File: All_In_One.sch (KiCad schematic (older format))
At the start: 20 parts

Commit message: complete schematic
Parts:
- removed D?: D_Zener, symbol Device:D_Zener
- removed D?: DIODE, symbol pspice:DIODE
- removed U? (x2): L298, symbol Prashant_library:L298
- added D? (x2): DIODE, symbol pspice:DIODE
- added D?: D_Zener, symbol Device:D_Zener
- added J?: Stepper_xaxis, symbol Connector:Conn_01x04_Female
- added J?: Stepper_yaxis, symbol Connector:Conn_01x04_Female
- added U? (x2): L298, symbol l298:L298
- A?: value Pololu_Breakout_A4988 -> Y_AXIS
- A?: value Pololu_Breakout_A4988 -> X_AXIS
- J?: value Conn_01x04_Female -> Bluetooth
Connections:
- net labels added: +12V, +24V, +5V, M0_1, M0_2, M0_EN, M0_IN1, M0_IN2, M1_1, M1_2, M1_EN, M1_IN1, M1_IN2, M2_1, M2_2, M2_EN, M2_IN1, M2_IN2, M3_1, M3_2, M3_EN, M3_IN1, M3_IN2, P_BACK, P_DOWN, P_FRONT, P_LEFT, P_RIGHT, P_UP, RX, TX, X_1A, X_1B, X_2A, X_2B, Y_1A, Y_1B, Y_2A, Y_2B, dirx, diry, en_x, en_y, stepx, stepy
- net labels removed: 12V, 24V, 5V
- wire segments 34 -> 125
- no-connect marks 0 -> 1
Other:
- note added: "5V REGULATOR"
- note added: "ARDUINO CONTROLLER\n"
- note added: "ARM PROXY\n"
- note added: "BASE MOTOR DRIVER"
- note added: "BASE PROXY\n"
- note added: "BLUETOOTH"
- note added: "STEPPER DRIVER ( A4988 )\n"
- note added: "STEPPER MOTOR\n"
- moved on the sheet: 1.2k

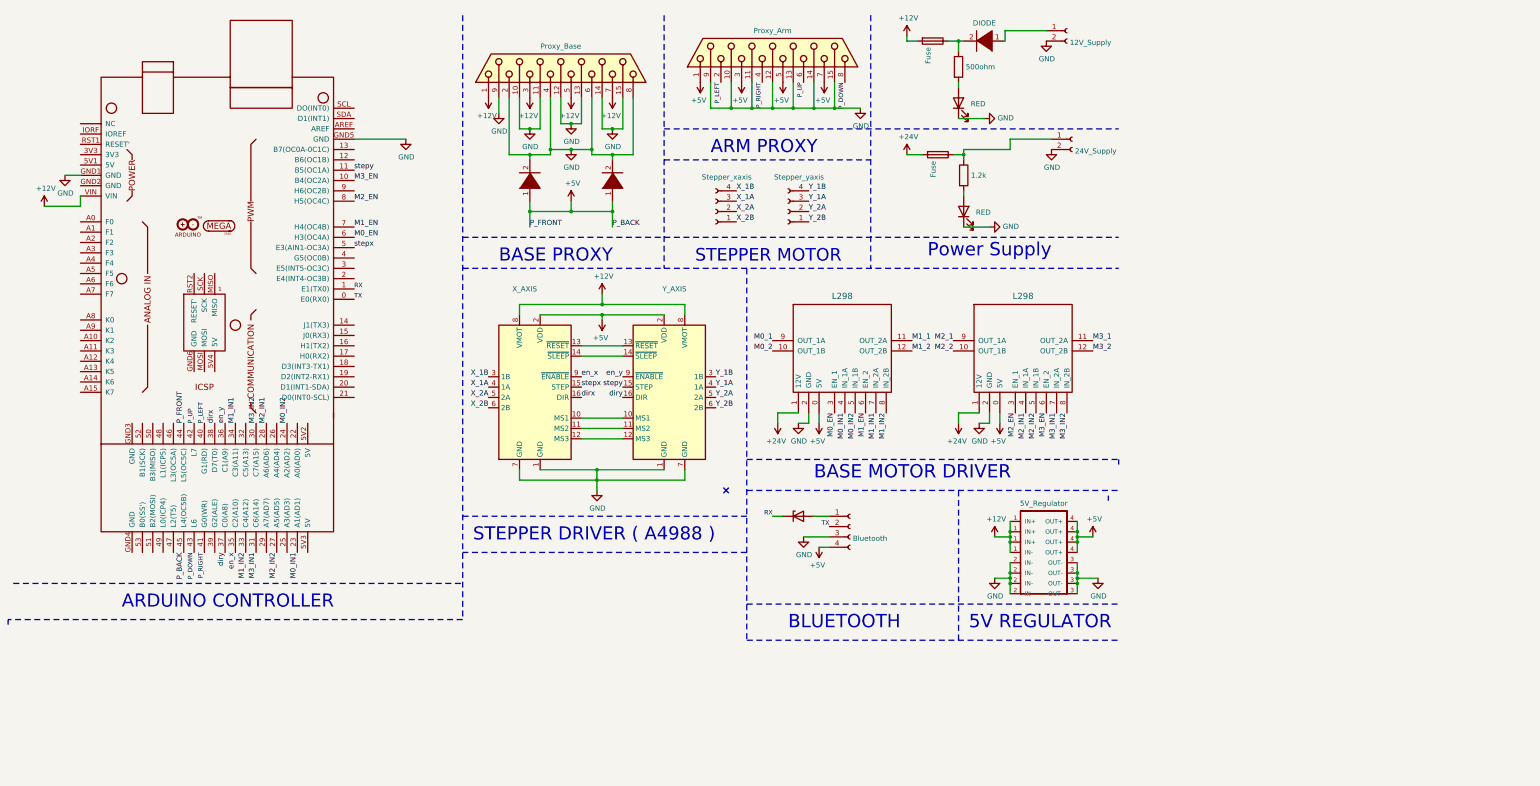
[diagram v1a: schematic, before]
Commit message: seperate ground for base motor and rest using opto-coupler
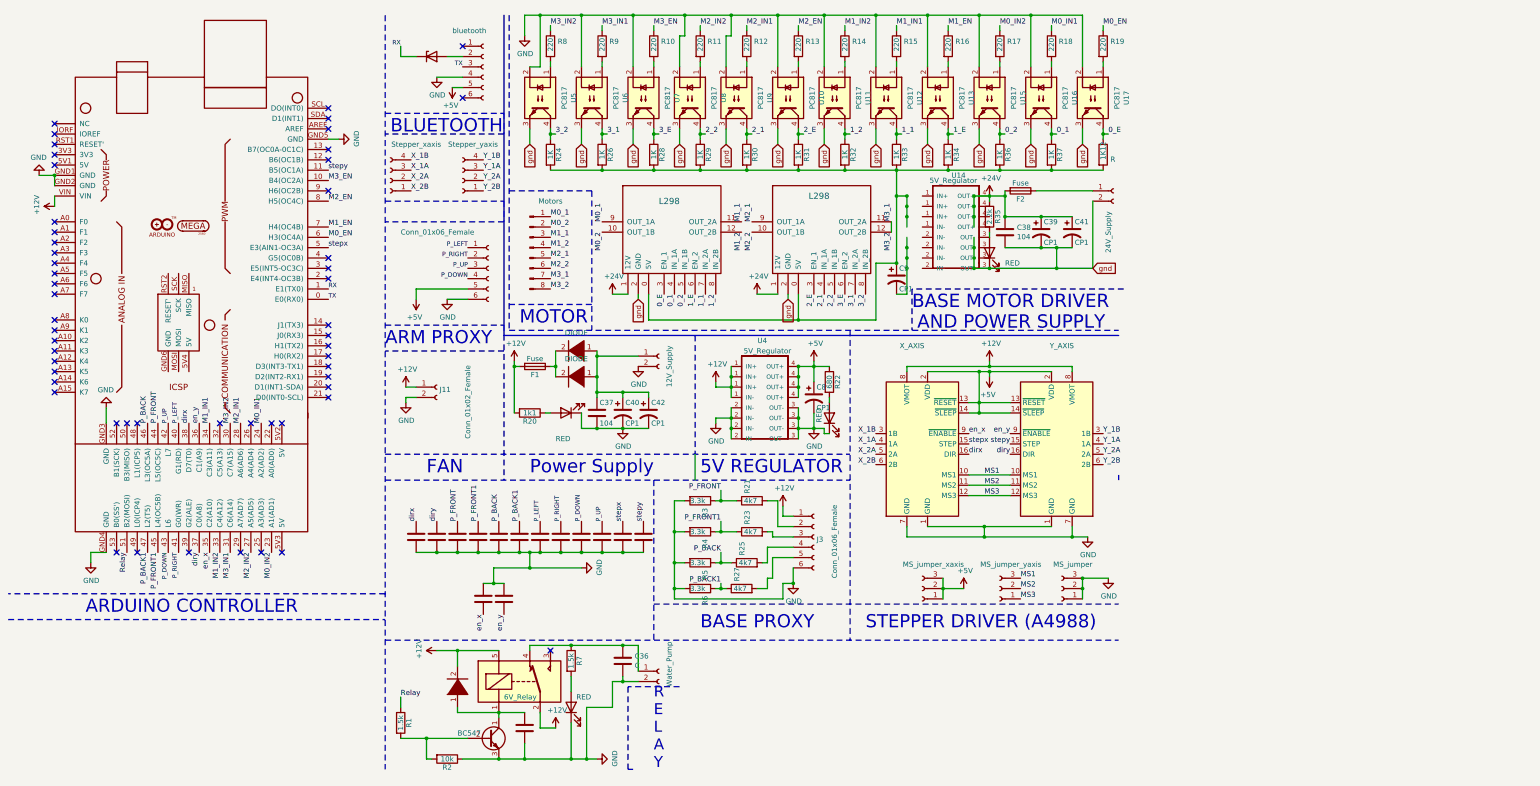
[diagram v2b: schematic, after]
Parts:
- removed D? (x2): DIODE, symbol pspice:DIODE
- removed J?: Bluetooth, symbol Connector:Conn_01x04_Female
- removed J?: Proxy_Base, symbol Connector:DB15_Female
- removed J?: Proxy_Arm, symbol Connector:DB15_Female
- added 1K12: R, modFiles:Resistor_small, symbol Device:R
- added C1, C13, C15, C2, C25, C27, C29, C3, C31, C33, C35, C36, C4, C5, C6, C7: C, modFiles:Capacitor_Disc_Small, symbol Device:C
- added C37, C38: 104, modFiles:Capacitor_Disc_Small, symbol Device:C
- added C39, C42: CP1, modFiles:Capacitor_10uF, symbol Device:CP1
- added C40, C41, C8, C9: CP1, modFiles:Capacitor_1000uF, symbol Device:CP1
- added D1, D3: DIODE, modFiles:Diode_Medium, symbol pspice:DIODE
- added D11, D2: RED, modFiles:LED_D3.0mm, symbol Device:LED
- added J1: MS_jumper_xaxis, symbol Connector:Conn_01x03_Female
- added J10: Motors, symbol Connector:Conn_01x08_Male
- added J11: Conn_01x02_Female, symbol Connector:Conn_01x02_Female
- added J2: MS_jumper_yaxis, symbol Connector:Conn_01x03_Female
- added J3, J8: Conn_01x06_Female, symbol Connector:Conn_01x06_Female
- added J4: Water_Pump, symbol Connector:Conn_01x02_Female
- added J5: MS_jumper, symbol Connector:Conn_01x03_Female
- added J9: bluetooth, symbol Connector:Conn_01x06_Female
- added Q1: BC547, Package_TO_SOT_THT:TO-92_Inline, symbol Transistor_BJT:BC547
- added R1, R7: 1.5k, modFiles:Resistor_small, symbol Device:R
- added R10, R11, R12, R13, R14, R15, R16, R17, R18, R19, R8, R9: 220, modFiles:Resistor_small, symbol Device:R
- added R2: 10k, modFiles:Resistor_small, symbol Device:R
- added R21, R23, R25, R27: 4k7, modFiles:Resistor_small, symbol Device:R
- added R22: 680, modFiles:Resistor_small, symbol Device:R
- added R24, R26, R28, R29, R30, R31, R32, R33, R34, R36, R37: 1K, modFiles:Resistor_small, symbol Device:R
- added R3, R4, R5, R6: 3.3k, modFiles:Resistor_small, symbol Device:R
- added Rly1: 6V_Relay, symbol Prashant_library:6V_Relay
- added U10, U11, U12, U13, U15, U16, U17, U5, U6, U7, U8, U9: PC817, Package_DIP:DIP-4_W7.62mm, symbol Isolator:PC817
- added U14: 5V_Regulator, modFiles:Buck 5A, symbol BUCK_Controller:BUCK
- A1, A2: renamed from A?; footprint Module:Pololu_Breakout-16_15.2x20.3mm -> modFiles:A4998
- D10: renamed from D?; footprint (none) -> modFiles:Diode_Medium
- D7: renamed from D?; footprint (none) -> Diode_THT:D_T-1_P5.08mm_Horizontal
- D8, D9: renamed from D?; footprint (none) -> modFiles:LED_D3.0mm
- F1, F2: renamed from F?; footprint (none) -> modFiles:Fuse_Holder
- R20: renamed from 500ohm; value R -> 1k1; footprint (none) -> modFiles:Resistor_small
- R35: renamed from 1.2k; value R -> 2.2k; footprint (none) -> modFiles:Resistor_small
- U2, U3: renamed from U?; footprint (none) -> modFiles:L298
- U4: renamed from U?; footprint (none) -> modFiles:Buck_Regulator
- d1: renamed from d; footprint (none) -> modFiles:Solar_Connector
- d2: renamed from d?; footprint (none) -> modFiles:Solar_Connector
- gave numbers to parts that had none: 3
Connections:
- net M3_2 is gone; now on net M3_1: U3.12 (OUT_2B)
- net +12V: now also R20.2, D1.2 (A), J11.1 (Pin_1), J3.1 (Pin_1), Rly1.2, Rly1.5
- net +24V: now also R35.1, C38.1, C39.1, C41.1, U14.4 (OUT+)
- net +5V: now also A1.13 (~RESET), A1.14 (~SLEEP), A2.13 (~RESET), A2.14 (~SLEEP), C8.1, J1.1 (Pin_1), J1.2 (Pin_2), J1.3 (Pin_3), J8.5 (Pin_5), J9.5 (Pin_5), R22.1; no longer U1.44 (L5(OC5C)), U1.45 (L4(OC5B)), U2.0 (5V), U3.0 (5V)
- net GND: now also U1.GND2 (GND), U1.GND3 (GND), U1.GND4 (GND), C1.2, C13.2, C15.2, C2.2, C25.2, C27.2, C29.2, C3.2, C31.2, C33.2, C35.2, C36.2, C37.2, C4.2, C40.2, C42.2, C5.2, C6.2, C7.2, C8.2, D11.1 (K), D2.1 (K), J11.2 (Pin_2), J3.6 (Pin_6), J4.2 (Pin_2), J5.1 (Pin_1), J5.2 (Pin_2), J5.3 (Pin_3), J8.6 (Pin_6), J9.4 (Pin_4), Q1.3 (E), R2.1, R3.2, R4.2, R5.2, R6.2, U10.2, U11.2, U12.2, U13.2, U15.2, U16.2, U17.2, U5.2, U6.2, U7.2, U8.2, U9.2; no longer D8.1 (K), U2.2 (GND), U3.2 (GND), d2.2 (Pin_2)
- net M0_1: now also J10.1 (Pin_1)
- net M0_2: now also J10.2 (Pin_2)
- net M0_EN: now also R19.1; no longer U2.3 (EN_1)
- net M0_IN1: now also U1.24 (A2(AD2)), R18.1; no longer U1.23 (A1(AD1)), U2.4 (IN_1A)
- net M0_IN2: now also U1.23 (A1(AD1)), R17.1; no longer U1.24 (A2(AD2)), U2.5 (IN_1B)
- net M1_1: now also J10.3 (Pin_3)
- net M1_2: now also J10.4 (Pin_4)
- net M1_EN: now also R16.1; no longer U2.6 (EN_2)
- net M1_IN1: now also R15.1; no longer U2.7 (IN_2A)
- net M1_IN2: now also R14.1; no longer U2.8 (IN_2B)
- net M2_1: now also J10.5 (Pin_5)
- net M2_2: now also J10.6 (Pin_6)
- net M2_EN: now also R13.1; no longer U3.3 (EN_1)
- net M2_IN1: now also R12.1; no longer U3.4 (IN_1A)
- net M2_IN2: now also R11.1; no longer U3.5 (IN_1B)
- net M3_1: now also J10.7 (Pin_7), J10.8 (Pin_8)
- net M3_EN: now also R10.1; no longer U3.6 (EN_2)
- net M3_IN1: now also R9.1; no longer U3.7 (IN_2A)
- net M3_IN2: now also R8.1; no longer U3.8 (IN_2B)
- net P_DOWN: now also C29.1, J8.4 (Pin_4)
- net P_LEFT: now also C25.1, J8.1 (Pin_1)
- net P_RIGHT: now also C27.1, J8.2 (Pin_2)
- net P_UP: now also C31.1, J8.3 (Pin_3)
- net TX: now also J9.3 (Pin_3)
- net dirx: now also C13.1
- net diry: now also C15.1
- net en_x: now also C3.1
- net en_y: now also C1.1
- net stepx: now also C33.1
- net stepy: now also C35.1
- net at D7.2 (A): now also J9.2 (Pin_2)
- net at D10.2 (A), F1.1: now also D3.2 (A); no longer R20.1
- net at D10.1 (K), d1.1 (Pin_1): now also C37.1, C40.1, C42.1, D3.1 (K)
- net MS1: now reaches A1.10 (MS1), A2.10 (MS1)
- net MS1: now also J2.3 (Pin_3)
- net MS2: now reaches A1.11 (MS2), A2.11 (MS2)
- net MS2: now also J2.2 (Pin_2)
- net MS3: now reaches A1.12 (MS3), A2.12 (MS3)
- net MS3: now also J2.1 (Pin_1)
- net at D9.2 (A): now also R20.1; no longer R20.2
- net at F2.1, d2.1 (Pin_1): no longer R35.1
- net at D8.2 (A), R35.2: now also U14.3 (OUT-)
- net P_BACK: now reaches U1.46 (L3(OC5A))
- net P_BACK: now also C5.1, R25.1, R5.1
- net P_BACK1: now reaches U1.47 (L2(T5))
- net P_BACK1: now also C6.1, R27.1, R6.1
- net Relay: now reaches U1.51 (B2(MOSI))
- net Relay: now also R1.1
- new net: 1K12.2, C9.1, R24.2, R26.2, R28.2, R29.2, R30.2, R31.2, R32.2, R33.2, R34.2, R36.2, R37.2, U2.0 (5V), U3.0 (5V)
- new net: R19.2, U17.1
- new net: D11.2 (A), R22.2
- new net: R18.2, U16.1
- new net: R17.2, U15.1
- new net: R16.2, U13.1
- new net: R15.2, U12.1
- new net: R14.2, U11.1
- new net: R13.2, U10.1
- new net: R12.2, U9.1
- new net: R11.2, U8.1
- new net: R10.2, U7.1
- new net: R9.2, U6.1
- new net: R8.2, U5.1
- new net: C7.1, D1.1 (K), Q1.1 (C), Rly1.1
- new net: C36.1, J4.1 (Pin_1), R7.1, Rly1.4
- new net: Q1.2 (B), R1.2, R2.2
- new net: D2.2 (A), R7.2
- new net: J3.2 (Pin_2), R21.2
- new net: J3.3 (Pin_3), R23.2
- new net: J3.4 (Pin_4), R25.2
- new net: J3.5 (Pin_5), R27.2
- new net 0_1: R37.1, U16.4, U2.4 (IN_1A)
- new net 0_2: R36.1, U15.4, U2.5 (IN_1B)
- new net 0_E: 1K12.1, U17.4, U2.3 (EN_1)
- new net 1_1: R33.1, U12.4, U2.7 (IN_2A)
- new net 1_2: R32.1, U11.4, U2.8 (IN_2B)
- new net 1_E: R34.1, U13.4, U2.6 (EN_2)
- new net 2_1: R30.1, U3.4 (IN_1A), U9.4
- new net 2_2: R29.1, U3.5 (IN_1B), U8.4
- new net 2_E: R31.1, U10.4, U3.3 (EN_1)
- new net 3_1: R26.1, U3.7 (IN_2A), U6.4
- new net 3_2: R24.1, U3.8 (IN_2B), U5.4
- new net 3_E: R28.1, U3.6 (EN_2), U7.4
- new net P_FRONT: C2.1, R21.1, R3.1, U1.44 (L5(OC5C))
- new net P_FRONT1: C4.1, R23.1, R4.1, U1.45 (L4(OC5B))
- new net gnd: C38.2, C39.2, C41.2, D8.1 (K), U10.3, U11.3, U12.3, U13.3, U14.3 (OUT-), U15.3, U16.3, U17.3, U2.2 (GND), U3.2 (GND), U5.3, U6.3, U7.3, U8.3, U9.3, d2.2 (Pin_2)
- no-connect marks 1 -> 54
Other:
- note added: "AND POWER SUPPLY\n"
- note added: "FAN\n"
- note added: "MOTOR"
- note added: "R\nE\nL\nA\nY\n"
- note added: "STEPPER DRIVER (A4988)\n"
- note removed: "STEPPER DRIVER ( A4988 )\n"
- note removed: "STEPPER MOTOR\n"
- moved on the sheet: R20, R35

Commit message: started joining tracks
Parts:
- J1, J2, J5: footprint (none) -> Connector_PinHeader_2.54mm:PinHeader_1x03_P2.54mm_Vertical
- J10: footprint (none) -> 0_18:New_conn_1x8
- J11: value Conn_01x02_Female -> Fan; footprint (none) -> 0_18:New_conn_1x2
- J3: value Conn_01x06_Female -> Base_Proxy; footprint (none) -> 0_18:New_conn_1x6
- J4: footprint (none) -> 0_18:New_conn_1x2
- J6, J7: footprint (none) -> 0_18:New_conn_1x4
- J8: value Conn_01x06_Female -> Arm_Proxy; footprint (none) -> 0_18:New_conn_1x6
- J9: footprint (none) -> modFiles:bluetooth
- Rly1: footprint (none) -> modFiles:Relay_6V
- U2, U3: footprint modFiles:L298 -> 0_18:saju_____L298
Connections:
- net +24V: now also R35.2; no longer R35.1
- net at 1K12.2, C9.1, R24.2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: now also U14.1 (IN-)
- net at C9.2: now also U14.2 (IN-)
- new net: D8.2 (A), R35.1
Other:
- note added: "ARM MOTOR\n\n"
- moved on the sheet: R35
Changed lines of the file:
@@
 L Device:R R35
 U 1 1 5F1E58AB
-P 9950 2450
-F 0 "R35" V 10030 2450 50  0000 C CNN
-F 1 "2.2k" V 9950 2450 50  0000 C CNN
-F 2 "modFiles:Resistor_small" V 9880 2450 50  0001 C CNN
-F 3 "" H 9950 2450 50  0001 C CNN
-	1    9950 2450
-	1    0    0    -1
+P 10550 2100
+F 0 "R35" V 10630 2100 50  0000 C CNN
+F 1 "2.2k" V 10550 2100 50  0000 C CNN
+F 2 "modFiles:Resistor_small" V 10480 2100 50  0001 C CNN
+F 3 "" H 10550 2100 50  0001 C CNN
+	1    10550 2100
+	0    1    1    0
 $EndComp
 $Comp
 L Device:LED D8
 U 1 1 5F1E58B4
-P 9950 2800
-F 0 "D8" V 9988 2682 50  0001 R CNN
-F 1 "RED" V 9850 2650 50  0000 R CNN
-F 2 "modFiles:LED_D3.0mm" H 9950 2800 50  0001 C CNN
-F 3 "~" H 9950 2800 50  0001 C CNN
-	1    9950 2800
-	0    -1   -1   0
+P 10900 2100
+F 0 "D8" V 10938 1982 50  0001 R CNN
+F 1 "RED" V 10800 1950 50  0000 R CNN
+F 2 "modFiles:LED_D3.0mm" H 10900 2100 50  0001 C CNN
+F 3 "~" H 10900 2100 50  0001 C CNN
+	1    10900 2100
+	-1   0    0    1
 $EndComp
 Wire Wire Line
@@
 F 0 "J6" H 4044 1675 50  0001 C CNN
 F 1 "Stepper_xaxis" H 3900 1750 50  0000 C CNN
-F 2 "" H 4150 2100 50  0001 C CNN
+F 2 "0_18:New_conn_1x4" H 4150 2100 50  0001 C CNN
 F 3 "~" H 4150 2100 50  0001 C CNN
 	1    4150 2100
@@
 F 0 "J7" H 4744 1675 50  0001 C CNN
 F 1 "Stepper_yaxis" H 4750 1750 50  0000 C CNN
-F 2 "" H 4850 2100 50  0001 C CNN
+F 2 "0_18:New_conn_1x4" H 4850 2100 50  0001 C CNN
 F 3 "~" H 4850 2100 50  0001 C CNN
 	1    4850 2100
@@
 F 0 "U2" H 6875 3137 60  0001 C CNN
 F 1 "L298" H 6850 2800 60  0000 C CNN
-F 2 "modFiles:L298" H 6850 2550 60  0001 C CNN
+F 2 "0_18:saju_____L298" H 6850 2550 60  0001 C CNN
 F 3 "" H 6850 2550 60  0001 C CNN
 	1    6850 2550
@@
 F 0 "J9" H 5077 976 50  0001 L CNN
 F 1 "bluetooth" H 4750 1350 50  0000 L CNN
-F 2 "" H 5050 1000 50  0001 C CNN
+F 2 "modFiles:bluetooth" H 5050 1000 50  0001 C CNN
 F 3 "~" H 5050 1000 50  0001 C CNN
 	1    5050 1000
@@
 F 0 "J10" H 5606 3228 50  0001 C CNN
 F 1 "Motors" H 5700 3200 50  0000 C CNN
-F 2 "" H 5500 2750 50  0001 C CNN
+F 2 "0_18:New_conn_1x8" H 5500 2750 50  0001 C CNN
 F 3 "~" H 5500 2750 50  0001 C CNN
 	1    5500 2750
@@
 F 0 "J2" H 9944 5725 50  0001 C CNN
 F 1 "MS_jumper_yaxis" H 9944 5816 50  0000 C CNN
-F 2 "" H 10050 6050 50  0001 C CNN
+F 2 "Connector_PinHeader_2.54mm:PinHeader_1x03_P2.54mm_Vertical" H 10050 6050 50  0001 C CNN
 F 3 "~" H 10050 6050 50  0001 C CNN
 	1    10050 6050
@@
 F 0 "J5" H 10544 5725 50  0001 C CNN
 F 1 "MS_jumper" H 10544 5816 50  0000 C CNN
-F 2 "" H 10650 6050 50  0001 C CNN
+F 2 "Connector_PinHeader_2.54mm:PinHeader_1x03_P2.54mm_Vertical" H 10650 6050 50  0001 C CNN
 F 3 "~" H 10650 6050 50  0001 C CNN
 	1    10650 6050
@@
 P 5100 2950
 F 0 "J8" H 5127 2926 50  0001 L CNN
-F 1 "Conn_01x06_Female" H 4250 3300 50  0000 L CNN
-F 2 "" H 5100 2950 50  0001 C CNN
+F 1 "Arm_Proxy" H 4250 3300 50  0000 L CNN
+F 2 "0_18:New_conn_1x6" H 5100 2950 50  0001 C CNN
 F 3 "~" H 5100 2950 50  0001 C CNN
 	1    5100 2950
@@
 F 0 "Rly1" H 5830 7396 50  0001 L CNN
 F 1 "6V_Relay" H 5250 7200 50  0000 L CNN
-F 2 "" H 5850 7300 50  0001 L CNN
+F 2 "modFiles:Relay_6V" H 5850 7300 50  0001 L CNN
 F 3 "" H 5400 6950 50  0000 C CNN
 	1    5200 7150
@@
 F 0 "J4" H 6777 6826 50  0001 L CNN
 F 1 "Water_Pump" V 6850 6700 50  0000 L CNN
-F 2 "" H 6750 6850 50  0001 C CNN
+F 2 "0_18:New_conn_1x2" H 6750 6850 50  0001 C CNN
 F 3 "~" H 6750 6850 50  0001 C CNN
 	1    6750 6850
@@
 Wire Wire Line
 	10100 2200 10100 2250
-Wire Wire Line
-	9950 2250 9950 2300
 Connection ~ 9950 2250
 Wire Wire Line
@@
 Wire Wire Line
 	9950 2950 10600 2950
-Wire Wire Line
-	9950 2600 9950 2650
 Connection ~ 10100 2450
 Connection ~ 10600 2750
@@
 F 0 "U3" H 8325 3137 60  0001 C CNN
 F 1 "L298" H 8300 2850 60  0000 C CNN
-F 2 "modFiles:L298" H 8300 2550 60  0001 C CNN
+F 2 "0_18:saju_____L298" H 8300 2550 60  0001 C CNN
 F 3 "" H 8300 2550 60  0001 C CNN
 	1    8300 2550
@@
 Wire Wire Line
 	10400 2200 10950 2200
-Wire Wire Line
-	10950 2300 10950 2950
 Wire Wire Line
 	9950 2250 10100 2250
@@
 P 8250 5550
 F 0 "J3" H 8277 5526 50  0000 L CNN
-F 1 "Conn_01x06_Female" V 8450 5150 50  0000 L CNN
-F 2 "" H 8250 5550 50  0001 C CNN
+F 1 "Base_Proxy" V 8450 5150 50  0000 L CNN
+F 2 "0_18:New_conn_1x6" H 8250 5550 50  0001 C CNN
 F 3 "~" H 8250 5550 50  0001 C CNN
 	1    8250 5550
@@
 P 4600 4100
 F 0 "J11" H 4627 4076 50  0000 L CNN
-F 1 "Conn_01x02_Female" V 4900 3600 50  0000 L CNN
-F 2 "" H 4600 4100 50  0001 C CNN
+F 1 "Fan" V 4900 3600 50  0000 L CNN
+F 2 "0_18:New_conn_1x2" H 4600 4100 50  0001 C CNN
 F 3 "~" H 4600 4100 50  0001 C CNN
 	1    4600 4100
@@
 F 0 "J1" H 9194 5725 50  0001 C CNN
 F 1 "MS_jumper_xaxis" H 9194 5816 50  0000 C CNN
-F 2 "" H 9300 6050 50  0001 C CNN
+F 2 "Connector_PinHeader_2.54mm:PinHeader_1x03_P2.54mm_Vertical" H 9300 6050 50  0001 C CNN
 F 3 "~" H 9300 6050 50  0001 C CNN
 	1    9300 6050
@@
 	9050 3200 9150 3200
 Connection ~ 9050 2250
-Connection ~ 9150 2250
-Wire Wire Line
-	9150 2250 9150 2350
-Connection ~ 9150 2350
-Wire Wire Line
-	9150 2450 9150 2550
-Wire Wire Line
-	9150 2350 9150 2450
-Connection ~ 9150 2450
-Wire Wire Line
-	9150 2650 9150 2750
-Connection ~ 9150 2750
-Wire Wire Line
-	9150 2750 9150 2850
-Connection ~ 9150 2850
-Wire Wire Line
-	9150 2950 9150 3200
-Wire Wire Line
-	9150 2850 9150 2950
-Connection ~ 9150 2950
-Wire Wire Line
-	9800 2650 9800 2750
-Connection ~ 9800 2750
-Wire Wire Line
-	9800 2850 9800 2950
-Wire Wire Line
-	9800 2750 9800 2850
-Connection ~ 9800 2850
-Connection ~ 9800 2950
-Connection ~ 9800 2250
-Wire Wire Line
-	9800 2250 9800 2350
-Connection ~ 9800 2350
-Wire Wire Line
-	9800 2450 9800 2550
-Wire Wire Line
-	9800 2350 9800 2450
-Connection ~ 9800 2450
 $Comp
 L BUCK_Controller:BUCK U14
@@
 	8850 2900 8850 3450
 Connection ~ 9050 2900
+Wire Wire Line
+	9150 2250 9150 2550
+Wire Wire Line
+	9800 2650 9800 2950
+Wire Wire Line
+	9800 2250 9800 2550
+Wire Wire Line
+	9150 2650 9150 3200
+Wire Wire Line
+	9300 2250 9300 2350
+Connection ~ 9300 2350
+Wire Wire Line
+	9300 2350 9300 2450
+Connection ~ 9300 2450
+Wire Wire Line
+	9300 2450 9300 2550
+Wire Wire Line
+	9300 2550 9150 2550
+Connection ~ 9300 2550
+Wire Wire Line
+	9300 2650 9300 2750
+Connection ~ 9300 2750
+Wire Wire Line
+	9300 2750 9300 2850
+Connection ~ 9300 2850
+Wire Wire Line
+	9300 2850 9300 2950
+Wire Wire Line
+	9150 2650 9300 2650
+Connection ~ 9300 2650
+Wire Wire Line
+	10700 2100 10750 2100
+Wire Wire Line
+	10400 2100 10100 2100
+Wire Wire Line
+	10100 2100 10100 2200
+Connection ~ 10100 2200
+Wire Wire Line
+	9950 2250 9950 2350
+Connection ~ 9950 2350
+Wire Wire Line
+	9950 2350 9950 2450
+Connection ~ 9950 2450
+Wire Wire Line
+	9950 2450 9950 2550
+Wire Wire Line
+	9950 2650 9950 2750
+Connection ~ 9950 2750
+Wire Wire Line
+	9950 2750 9950 2850
+Connection ~ 9950 2850
+Wire Wire Line
+	9950 2850 9950 2950
+Wire Wire Line
+	11050 2100 11200 2100
+Wire Wire Line
+	11200 2100 11200 2550
+Wire Wire Line
+	11200 2550 10950 2550
+Wire Wire Line
+	10950 2300 10950 2550
+Connection ~ 10950 2550
+Wire Wire Line
+	10950 2550 10950 2950
+Text Notes 4150 2700 0    127  ~ 0
+ARM MOTOR\n\n
 $EndSCHEMATC
